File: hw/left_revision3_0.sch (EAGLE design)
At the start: 64 parts, among them J2 CAN, X1 7A-20.000MAAJ-T

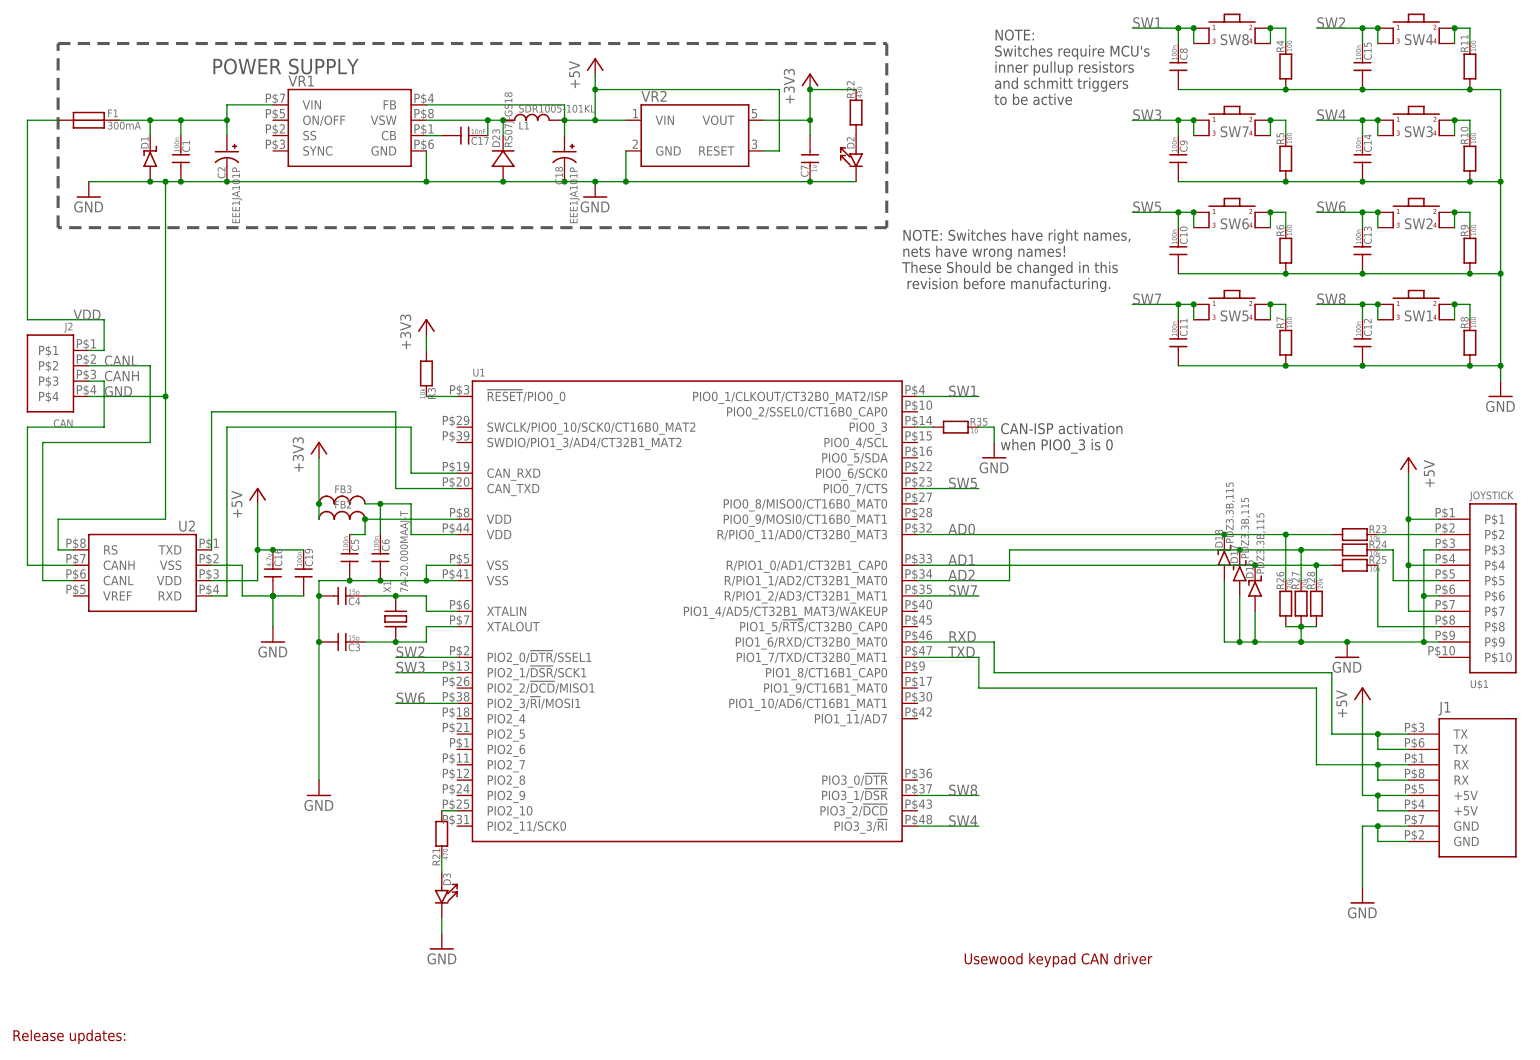
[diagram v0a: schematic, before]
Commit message: Add 2.0 and 3.0 HW versions
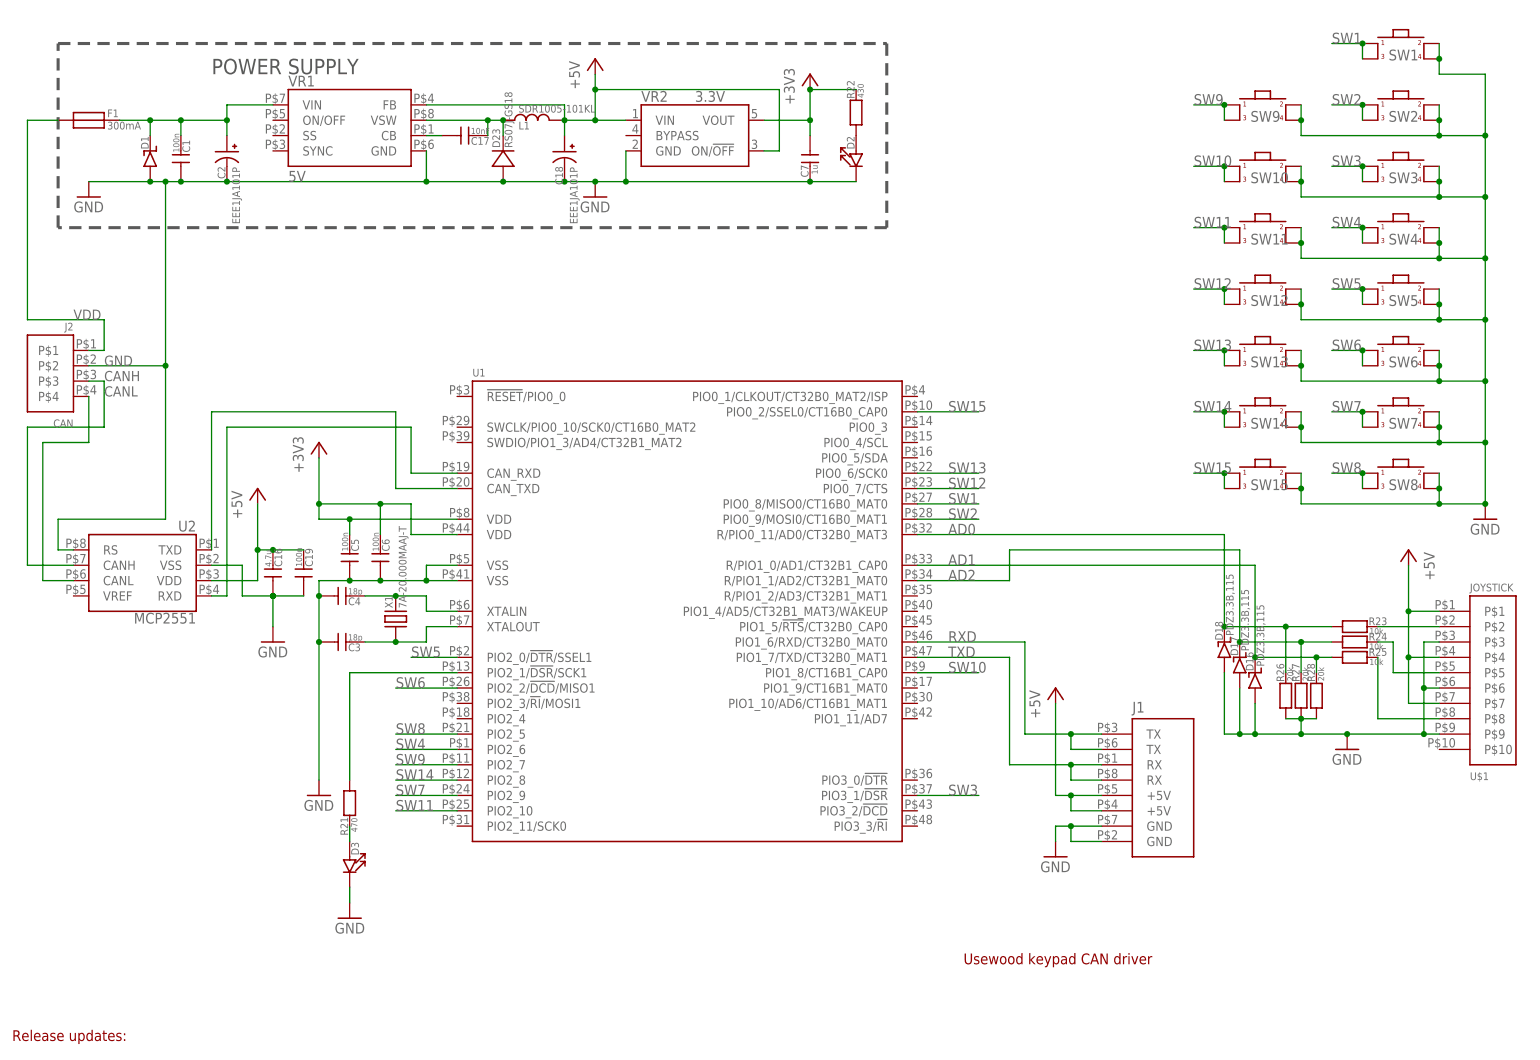
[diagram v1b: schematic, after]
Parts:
- removed C10, C11, C12, C13, C14, C15, C8, C9: 100n, usevolt:CAP0603_SILKSCREEN
- removed FB2, FB3: FERRITE0603_SILKSCREEN, usevolt:FERRITE0603_SILKSCREEN
- removed R10, R11, R4, R5, R6, R7, R8, R9: 100, usevolt:RES0604_SILKSCREEN
- removed R3: 10k, usevolt:RES0604_SILKSCREEN
- removed R35: 10, usevolt:RES0604_SILKSCREEN
- added SW10, SW11, SW12, SW13, SW14, SW15, SW9: (no value), usevolt:SWITCH_EVQP6L
- C1, C16, C17, C19, C5, C6, C7: device usevolt:CAP0603_SILKSCREEN -> usevolt:CAP_0603
- C3, C4: value 15p -> 18p; device usevolt:CAP0603_SILKSCREEN -> usevolt:CAP_0603
- D2, D3: device usevolt:LED0603_SILKSCREEN -> usevolt:LED_0603
- F1: device arm:FUSE100MA -> usevolt:FUSE_MC36204_100MA
- J1: device usevolt:HEADER_USART_2_TH -> usevolt:HEADER_USART_2_SMD
- J2: device arm:MOLEX_MICRO-FIT_4WAYTH -> usevolt:MOLEX_MICRO-FIT_4WAY_SMD
- R21, R22, R23, R24, R25, R26, R27, R28: device usevolt:RES0604_SILKSCREEN -> usevolt:RES_0603
- SW1, SW2, SW3, SW4, SW5, SW6, SW7, SW8: device arm:SWITCH12X12MM_CENTER_HOLE -> usevolt:SWITCH_EVQP6L
- U$1: device usevolt:MOLEX_MICRO-FIT_10WAYTH -> usevolt:MOLEX_MICRO-FIT_10WAY_SMD
- U2: value (none) -> MCP2551
- VR1: value (none) -> 5V
- VR2: value (none) -> 3.3V; device arm:LP2985SOP5 -> usevolt:REG_LP2985_SOP5
- X1: device arm:XTALSMD_5X3.2 -> usevolt:XTAL_7A-12.000MAAJ-T
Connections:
- removed net CAN_ISP: R35.P$1, U1.PIO0_3
- removed net N$1: C5.P$2, FB2.P$2, U1.VDD
- removed net N$12: R4.P$2, SW8.P$2, SW8.P$4
- removed net N$13: R5.P$2, SW7.P$2, SW7.P$4
- removed net N$14: R6.P$2, SW6.P$2, SW6.P$4
- removed net N$15: R11.P$2, SW4.P$2, SW4.P$4
- removed net N$16: R9.P$2, SW2.P$2, SW2.P$4
- removed net N$17: R10.P$2, SW3.P$2, SW3.P$4
- removed net N$18: R8.P$2, SW1.P$2, SW1.P$4
- removed net N$19: R7.P$2, SW5.P$2, SW5.P$4
- removed net N$26: C6.P$2, FB3.P$2, U1.VDD@2
- removed net RESET: R3.P$2, U1.!RESET!/PIO0_0
- new net SW10: SW10.P$1, SW10.P$3, U1.PIO1_8/CT16B1_CAP0
- new net SW11: SW11.P$1, SW11.P$3, U1.PIO2_10
- new net SW12: SW12.P$1, SW12.P$3, U1.PIO0_7/CTS
- new net SW13: SW13.P$1, SW13.P$3, U1.PIO0_6/SCK0
- new net SW14: SW14.P$1, SW14.P$3, U1.PIO2_8
- new net SW15: SW15.P$1, SW15.P$3, U1.PIO0_2/SSEL0/CT16B0_CAP0
- new net SW9: SW9.P$1, SW9.P$3, U1.PIO2_7
- net +3V3: now also C5.P$2, C6.P$2, U1.VDD, U1.VDD@2; no longer FB2.P$1, FB3.P$1, R3.P$1
- net +5V: now also VR2.ON/!OFF; no longer VR2.RESET
- net CANL: now also J2.P$4; no longer J2.P$2
- net GND: now also J2.P$2, SW1.P$2, SW1.P$4, SW10.P$2, SW10.P$4, SW11.P$2, SW11.P$4, SW12.P$2, SW12.P$4, SW13.P$2, SW13.P$4, SW14.P$2, SW14.P$4, SW15.P$2, SW15.P$4, SW2.P$2, SW2.P$4, SW3.P$2, SW3.P$4, SW4.P$2, SW4.P$4, SW5.P$2, SW5.P$4, SW6.P$2, SW6.P$4, SW7.P$2, SW7.P$4, SW8.P$2, SW8.P$4, SW9.P$2, SW9.P$4, U1.VSS@2; no longer C10.P$1, C11.P$1, C12.P$1, C13.P$1, C14.P$1, C15.P$1, C8.P$1, C9.P$1, J2.P$4, R10.P$1, R11.P$1, R35.P$2, R4.P$1, R5.P$1, R6.P$1, R7.P$1, R8.P$1, R9.P$1
- net N$2: now also U1.PIO2_1/!DSR!/SCK1; no longer U1.PIO2_10
- net SW1: now also SW1.P$1, SW1.P$3, U1.PIO0_8/MISO0/CT16B0_MAT0; no longer C8.P$2, SW8.P$1, SW8.P$3, U1.PIO0_1/CLKOUT/CT32B0_MAT2/ISP
- net SW2: now also SW2.P$1, SW2.P$3, U1.PIO0_9/MOSI0/CT16B0_MAT1; no longer C15.P$2, SW4.P$1, SW4.P$3, U1.PIO2_0/!DTR!/SSEL1
- net SW3: now also SW3.P$1, SW3.P$3, U1.PIO3_1/!DSR; no longer C9.P$2, SW7.P$1, SW7.P$3, U1.PIO2_1/!DSR!/SCK1
- net SW4: now also SW4.P$1, SW4.P$3, U1.PIO2_6; no longer C14.P$2, SW3.P$1, SW3.P$3, U1.PIO3_3/!RI
- net SW5: now also SW5.P$1, SW5.P$3, U1.PIO2_0/!DTR!/SSEL1; no longer C10.P$2, SW6.P$1, SW6.P$3, U1.PIO0_7/CTS
- net SW6: now also SW6.P$1, SW6.P$3, U1.PIO2_2/!DCD!/MISO1; no longer C13.P$2, SW2.P$1, SW2.P$3, U1.PIO2_3/!RI!/MOSI1
- net SW7: now also SW7.P$1, SW7.P$3, U1.PIO2_9; no longer C11.P$2, SW5.P$1, SW5.P$3, U1.R/PIO1_2/AD3/CT32B1_MAT1
- net SW8: now also SW8.P$1, SW8.P$3, U1.PIO2_5; no longer C12.P$2, SW1.P$1, SW1.P$3, U1.PIO3_1/!DSR
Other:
- note removed: "CAN-ISP activation when PIO0_3 is 0"
- note removed: "NOTE: Switches have right names, nets have wrong names! These Should be changed in this revision before manufacturing."
- note removed: "NOTE: Switches require MCU's inner pullup resistors and schmitt triggers to be active"
- moved on the sheet: D16, D17, D18, D3, J1, R21, R23, R24, R25, R26, R27, R28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
